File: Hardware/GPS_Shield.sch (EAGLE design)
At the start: 52 parts, among them J1 ARDUINO_R3_SHIELD, J2 USD_CONNECTOR, U1 APK2112-3.3V, U2 GP3906-TLP, U3 TXB0108

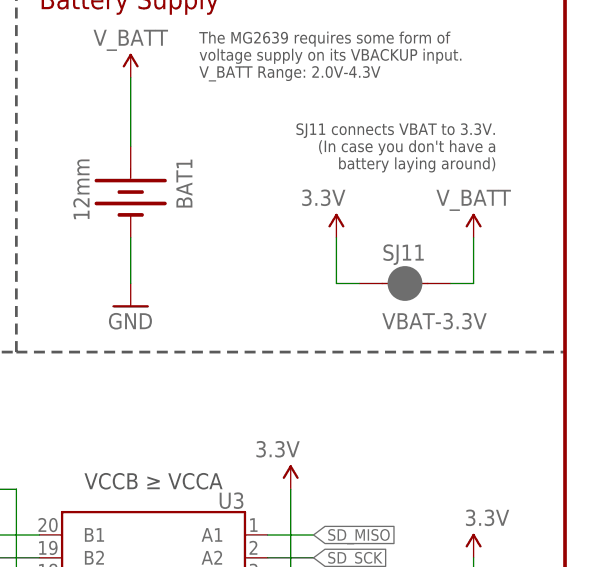
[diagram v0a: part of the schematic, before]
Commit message: Default SJ11 to open.
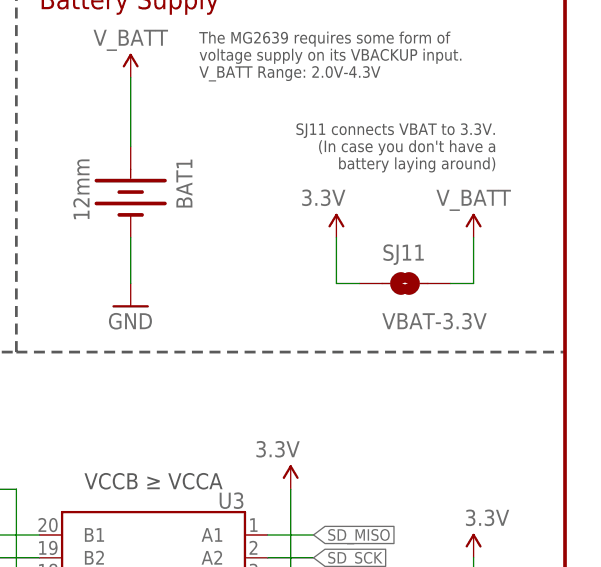
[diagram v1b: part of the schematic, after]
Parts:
- SJ11: device SparkFun-Passives:JUMPER-PAD-2-NC_BY_PASTE -> SparkFun-Passives:JUMPER-PAD-2-NOYES_SILK
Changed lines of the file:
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@@
 <part name="P+13" library="SparkFun" deviceset="3.3V" device=""/>
 <part name="GND19" library="SparkFun" deviceset="GND" device=""/>
-<part name="SJ11" library="SparkFun-Passives" deviceset="JUMPER-PAD-2-NC_BY_PASTE" device="" value="VBAT-3.3V"/>
+<part name="SJ11" library="SparkFun-Passives" deviceset="JUMPER-PAD-2-NO" device="YES_SILK" value="VBAT-3.3V"/>
 </parts>
 <sheets>

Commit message: Updating 12mm battery PROD_ID
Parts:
- BAT1: device SparkFun:BATTERY12MM -> SparkFun-Electromechanical:BATTERY12MM
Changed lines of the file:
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@@
 </classes>
 <parts>
-<part name="BAT1" library="SparkFun" deviceset="BATTERY" device="12MM" value="12mm"/>
+<part name="BAT1" library="SparkFun-Electromechanical" deviceset="BATTERY" device="12MM" value="12mm"/>
 <part name="GND16" library="SparkFun" deviceset="GND" device=""/>
 <part name="C3" library="SparkFun-Capacitors" deviceset="0.1UF-25V(+80/-20%)(0603)" device="" value="0.1uF"/>
